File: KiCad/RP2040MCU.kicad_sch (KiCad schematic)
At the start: 54 parts, among them J6 2.54mm header 01x20, J7 2.54mm header 01x20, J8 TSA343G00-250J2, J9 Conn_01x03_Male, Q1 SI2301B, U3 SOT-23-5 5.5V 3.3V 500mA, U4 RP2040, Y1 3225_4P

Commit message: routed onboard MCU
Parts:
- removed C7: 0.1uf 0402, Capacitor_SMD:C_0402_1005Metric, symbol Device:C
- removed R9: 220 0402, Resistor_SMD:R_0402_1005Metric, symbol Device:R
- removed TP1, TP2, TP3: TestPoint, EnvExtras:CustomTestPoint, symbol Connector:TestPoint
- J9: value Conn_01x03_Male -> C145960; footprint Connector_PinHeader_2.54mm:PinHeader_1x03_P2.54mm_Vertical -> Connector_JST:JST_SH_BM03B-SRSS-TB_1x03-1MP_P1.00mm_Vertical
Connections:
- net GND: now also USB1.13 (SHIELD)
- net GPIO17 renamed NCS/GPIO9
- net GPIO18 renamed SCLK/GPIO2
- net GPIO19 renamed MOSI/GPIO3
- net GPIO20 renamed MISO/GPIO4
- net GPIO21 renamed MOTION/GPIO1
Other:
- note removed: "Test points"

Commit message: I dont even remember what I changed.
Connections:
- net GPIO0 renamed ROT-B
- net GPIO1 renamed ROT-A
- net GPIO2 renamed MB-1-A
- net GPIO3 renamed MB-1-B
- net GPIO4 renamed MB-2-A
- net GPIO5 renamed MB-2-B
- net GPIO6 renamed MB-3-A
- net GPIO7 renamed MB-3-B
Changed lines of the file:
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@@
+    )
+  )
+  (global_label "MB-1-A" (shape input) (at 245.11 116.84 0) (fields_autoplaced)
+    (effects (font (size 1.27 1.27)) (justify left))
+    (property "Intersheet References" "${INTERSHEET_REFS}" (id 0) (at 255.8779 116.7606 0)
+      (effects (font (size 1.27 1.27)) (justify left) hide)
+    )
+  )
+  (global_label "MB-3-A" (shape input) (at 245.11 127 0) (fields_autoplaced)
+    (effects (font (size 1.27 1.27)) (justify left))
+    (property "Intersheet References" "${INTERSHEET_REFS}" (id 0) (at 255.8779 126.9206 0)
+      (effects (font (size 1.27 1.27)) (justify left) hide)
     )
   )
@@
     )
   )
+  (global_label "ROT-A" (shape input) (at 245.11 114.3 0) (fields_autoplaced)
+    (effects (font (size 1.27 1.27)) (justify left))
+    (property "Intersheet References" "${INTERSHEET_REFS}" (id 0) (at 253.9426 114.3794 0)
+      (effects (font (size 1.27 1.27)) (justify left) hide)
+    )
+  )
   (global_label "VSYS" (shape input) (at 66.04 44.45 0) (fields_autoplaced)
     (effects (font (size 0.508 0.508)) (justify left))
     (property "Intersheet References" "${INTERSHEET_REFS}" (id 0) (at 0 0 0)
       (effects (font (size 1.27 1.27)) hide)
+    )
+  )
+  (global_label "MB-3-B" (shape input) (at 245.11 129.54 0) (fields_autoplaced)
+    (effects (font (size 1.27 1.27)) (justify left))
+    (property "Intersheet References" "${INTERSHEET_REFS}" (id 0) (at 256.0593 129.4606 0)
+      (effects (font (size 1.27 1.27)) (justify left) hide)
     )
   )
@@
     )
   )
+  (global_label "MB-2-A" (shape input) (at 245.11 121.92 0) (fields_autoplaced)
+    (effects (font (size 1.27 1.27)) (justify left))
+    (property "Intersheet References" "${INTERSHEET_REFS}" (id 0) (at 255.8779 121.8406 0)
+      (effects (font (size 1.27 1.27)) (justify left) hide)
+    )
+  )
   (global_label "VBUS" (shape input) (at 71.12 54.61 180) (fields_autoplaced)
     (effects (font (size 1.1938 1.1938)) (justify right))
@@
     )
   )
+  (global_label "ROT-B" (shape input) (at 245.11 111.76 0) (fields_autoplaced)
+    (effects (font (size 1.27 1.27)) (justify left))
+    (property "Intersheet References" "${INTERSHEET_REFS}" (id 0) (at 254.1241 111.8394 0)
+      (effects (font (size 1.27 1.27)) (justify left) hide)
+    )
+  )
   (global_label "XOUT" (shape input) (at 165.1 152.4 180) (fields_autoplaced)
     (effects (font (size 1.27 1.27)) (justify right))
@@
     )
   )
+  (global_label "MB-1-B" (shape input) (at 245.11 119.38 0) (fields_autoplaced)
+    (effects (font (size 1.27 1.27)) (justify left))
+    (property "Intersheet References" "${INTERSHEET_REFS}" (id 0) (at 256.0593 119.3006 0)
+      (effects (font (size 1.27 1.27)) (justify left) hide)
+    )
+  )
+  (global_label "MB-2-B" (shape input) (at 245.11 124.46 0) (fields_autoplaced)
+    (effects (font (size 1.27 1.27)) (justify left))
+    (property "Intersheet References" "${INTERSHEET_REFS}" (id 0) (at 256.0593 124.3806 0)
+      (effects (font (size 1.27 1.27)) (justify left) hide)
+    )
+  )

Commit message: decided to work on this again | made PCB have reasonableish dimensions and moved mouse buttons to suitable positions
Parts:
- removed J6, J7: 2.54mm header 01x20, Connector_PinHeader_2.54mm:PinHeader_1x20_P2.54mm_Vertical, symbol Connector_Generic:Conn_01x20
- removed NT1: NetTie_2, NetTie:NetTie-2_SMD_Pad0.5mm, symbol Device:NetTie_2
- removed R4: 200 0603, Resistor_SMD:R_0603_1608Metric, symbol Device:R_Small
- removed R6: 1 0402, Resistor_SMD:R_0402_1005Metric, symbol Device:R_Small

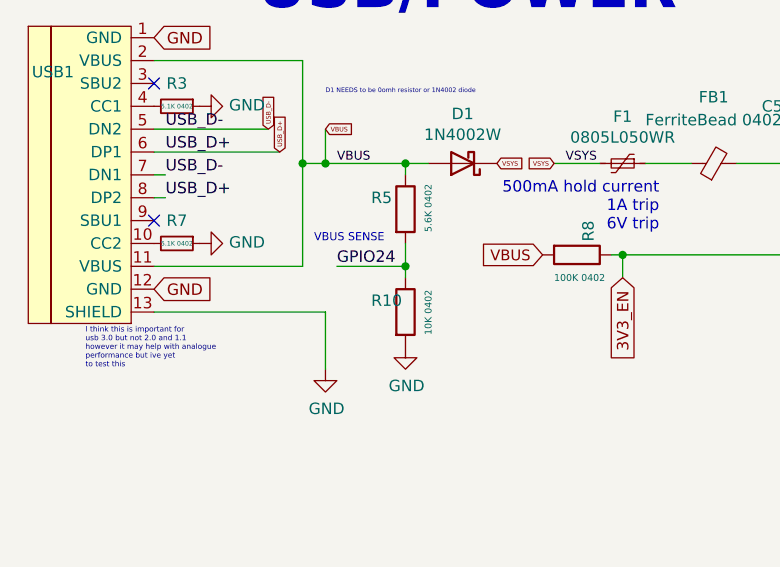
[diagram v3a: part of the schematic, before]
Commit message: routed some more traces
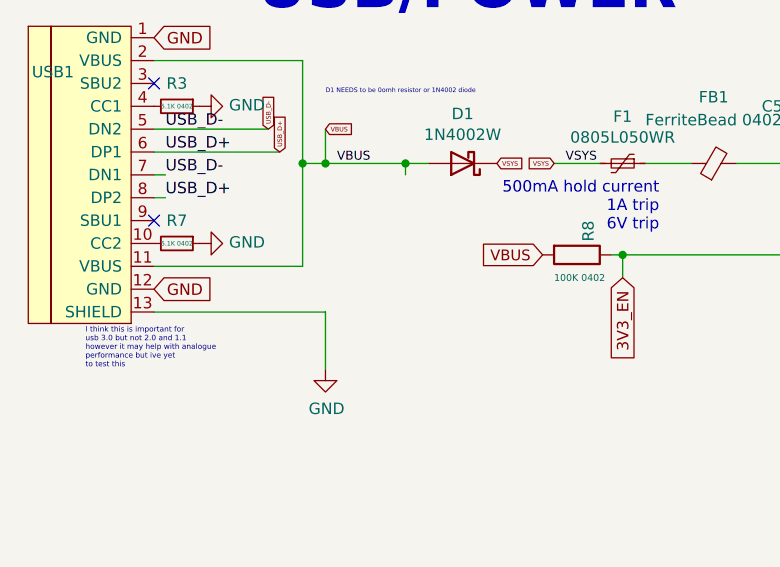
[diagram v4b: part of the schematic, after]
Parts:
- removed R10: 10K 0402, Resistor_SMD:R_0402_1005Metric, symbol Device:R
- removed R5: 5.6K 0402, Resistor_SMD:R_0402_1005Metric, symbol Device:R
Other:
- note removed: "VBUS SENSE"
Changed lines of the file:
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@@
   (junction (at 194.31 81.28) (diameter 0) (color 0 0 0 0)
-  )
-  (junction (at 55.88 55.88) (diameter 0) (color 0 0 0 0)
   )
   (junction (at 289.56 72.39) (diameter 0) (color 0 0 0 0)
@@
     (stroke (width 0) (type default) (color 0 0 0 0))
   )
-  (wire (pts (xy 55.88 55.88) (xy 55.88 57.15))
-    (stroke (width 0) (type default) (color 0 0 0 0))
-  )
   (wire (pts (xy 27.94 43.18) (xy 41.91 43.18))
     (stroke (width 0) (type default) (color 0 0 0 0))
@@
     (stroke (width 0) (type default) (color 0 0 0 0))
   )
-  (wire (pts (xy 55.88 53.34) (xy 55.88 55.88))
-    (stroke (width 0) (type default) (color 0 0 0 0))
-  )
   (wire (pts (xy 207.01 81.28) (xy 210.82 81.28))
     (stroke (width 0) (type default) (color 0 0 0 0))
@@
   )
   (wire (pts (xy 229.87 142.24) (xy 245.11 142.24))
-    (stroke (width 0) (type default) (color 0 0 0 0))
-  )
-  (wire (pts (xy 48.26 55.88) (xy 55.88 55.88))
     (stroke (width 0) (type default) (color 0 0 0 0))
   )
@@
     (effects (font (size 1.27 1.27)) (justify left bottom))
   )
-  (text "VBUS SENSE" (at 45.72 53.34 0)
-    (effects (font (size 0.9 0.9)) (justify left bottom))
-  )
   (text "2x 5.1K Resistors on the CC pins will = 5V@1.5A\nthis is the recomended default config for type-c"
     (at 15.24 19.05 0)
@@
   (label "GPIO9" (at 245.11 134.62 180)
     (effects (font (size 1.27 1.27)) (justify right bottom))
-  )
-  (label "GPIO24" (at 48.26 55.88 0)
-    (effects (font (size 1.27 1.27)) (justify left bottom))
   )
   (label "GPIO27_ADC1" (at 245.11 182.88 180)
@@
     (pin "1")
   )
-  (symbol (lib_id "Device:R") (at 55.88 60.96 0) (unit 1)
-    (in_bom yes) (on_board yes)
-    (property "Reference" "R10" (id 0) (at 52.07 59.69 0)
-      (effects (font (size 1.27 1.27)) (justify left))
-    )
-    (property "Value" "10K 0402" (id 1) (at 58.42 63.5 90)
-      (effects (font (size 0.762 0.762)) (justify left))
-    )
-    (property "Footprint" "Resistor_SMD:R_0402_1005Metric" (id 2) (at 54.102 60.96 90)
-      (effects (font (size 1.27 1.27)) hide)
-    )
-    (property "Datasheet" "" (id 3) (at 55.88 60.96 0)
-      (effects (font (size 1.27 1.27)) hide)
-    )
-    (property "LCSC" " " (id 4) (at 55.88 60.96 0)
-      (effects (font (size 1.27 1.27)) hide)
-    )
-    (pin "1")
-    (pin "2")
-  )
   (symbol (lib_id "Device:FerriteBead_Small") (at 90.17 44.45 90) (unit 1)
     (in_bom yes) (on_board yes) (fields_autoplaced)
@@
       (effects (font (size 1.27 1.27)) hide)
     )
-    (pin "1")
-    (pin "2")
-  )
-  (symbol (lib_id "power:GND") (at 55.88 64.77 0) (unit 1)
-    (in_bom yes) (on_board yes)
-    (property "Reference" "#PWR025" (id 0) (at 55.88 71.12 0)
-      (effects (font (size 1.27 1.27)) hide)
-    )
-    (property "Value" "GND" (id 1) (at 56.007 69.1642 0))
-    (property "Footprint" "" (id 2) (at 55.88 64.77 0)
-      (effects (font (size 1.27 1.27)) hide)
-    )
-    (property "Datasheet" "" (id 3) (at 55.88 64.77 0)
-      (effects (font (size 1.27 1.27)) hide)
-    )
-    (pin "1")
-  )
-  (symbol (lib_id "Device:R") (at 55.88 49.53 0) (unit 1)
-    (in_bom yes) (on_board yes)
-    (property "Reference" "R5" (id 0) (at 52.07 48.26 0)
-      (effects (font (size 1.27 1.27)) (justify left))
-    )
-    (property "Value" "5.6K 0402" (id 1) (at 58.42 52.07 90)
-      (effects (font (size 0.762 0.762)) (justify left))
-    )
-    (property "Footprint" "Resistor_SMD:R_0402_1005Metric" (id 2) (at 54.102 49.53 90)
-      (effects (font (size 1.27 1.27)) hide)
-    )
-    (property "Datasheet" "" (id 3) (at 55.88 49.53 0)
-      (effects (font (size 1.27 1.27)) hide)
-    )
-    (property "LCSC" " " (id 4) (at 55.88 49.53 0)
-      (effects (font (size 1.27 1.27)) hide)
-    )

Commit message: ran traces for parts previously left disconnected and moved about some to improve ease of routing and also shortened PCB down to 94mm along with slimmed width + mount holes
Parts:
- J9: footprint Connector_JST:JST_SH_BM03B-SRSS-TB_1x03-1MP_P1.00mm_Vertical -> Connector_PinHeader_1.27mm:PinHeader_1x03_P1.27mm_Vertical
